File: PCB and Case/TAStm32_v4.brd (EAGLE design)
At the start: 50 x 100 mm, 55 parts, among them CN1 330pF, CN2 330pF, CN3 330pF, CN4 330pF, IC1 74HCT3G07DP-Q100H, IC2 74HCT3G07DP-Q100H, IC3 74AVCH4T245PW,118, IC4 74AVCH4T245PW,118, J1 ZX62D-B-5PA8, J10 RJSSE538002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

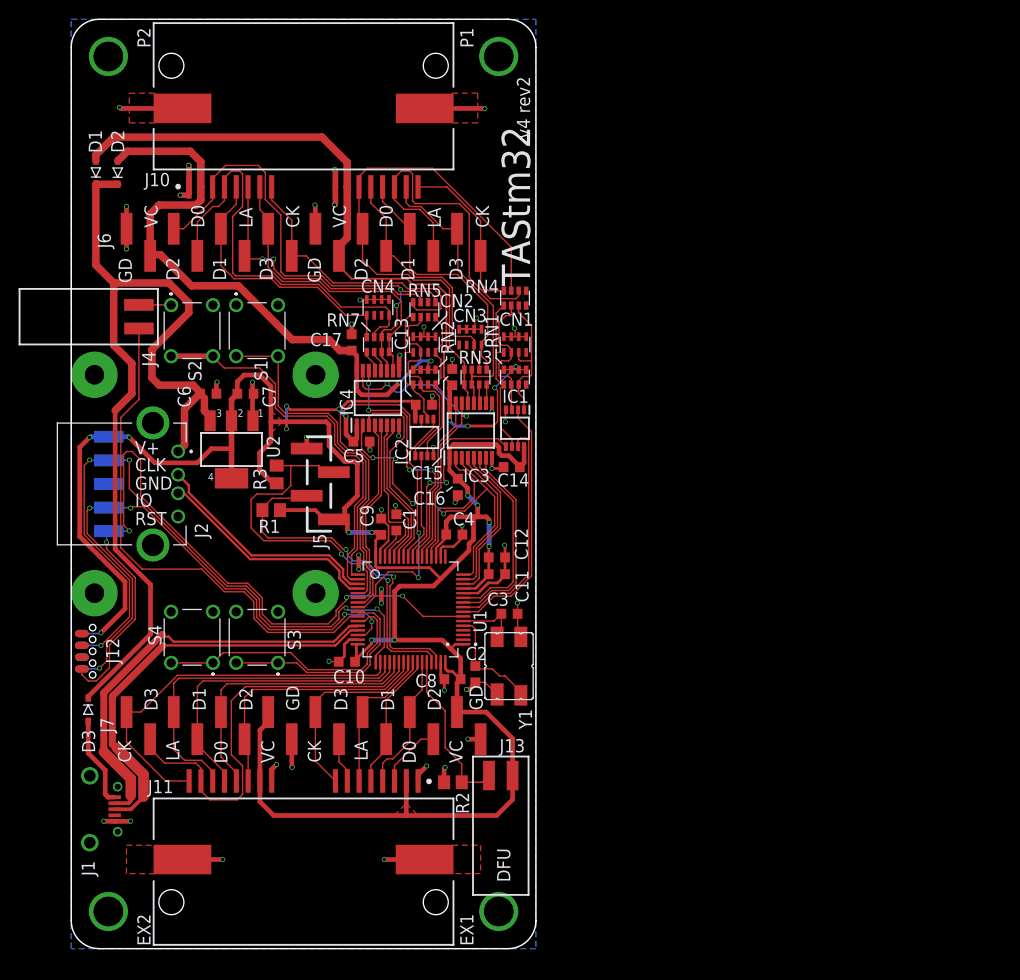
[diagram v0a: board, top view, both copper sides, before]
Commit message: more silkscreen cleanup
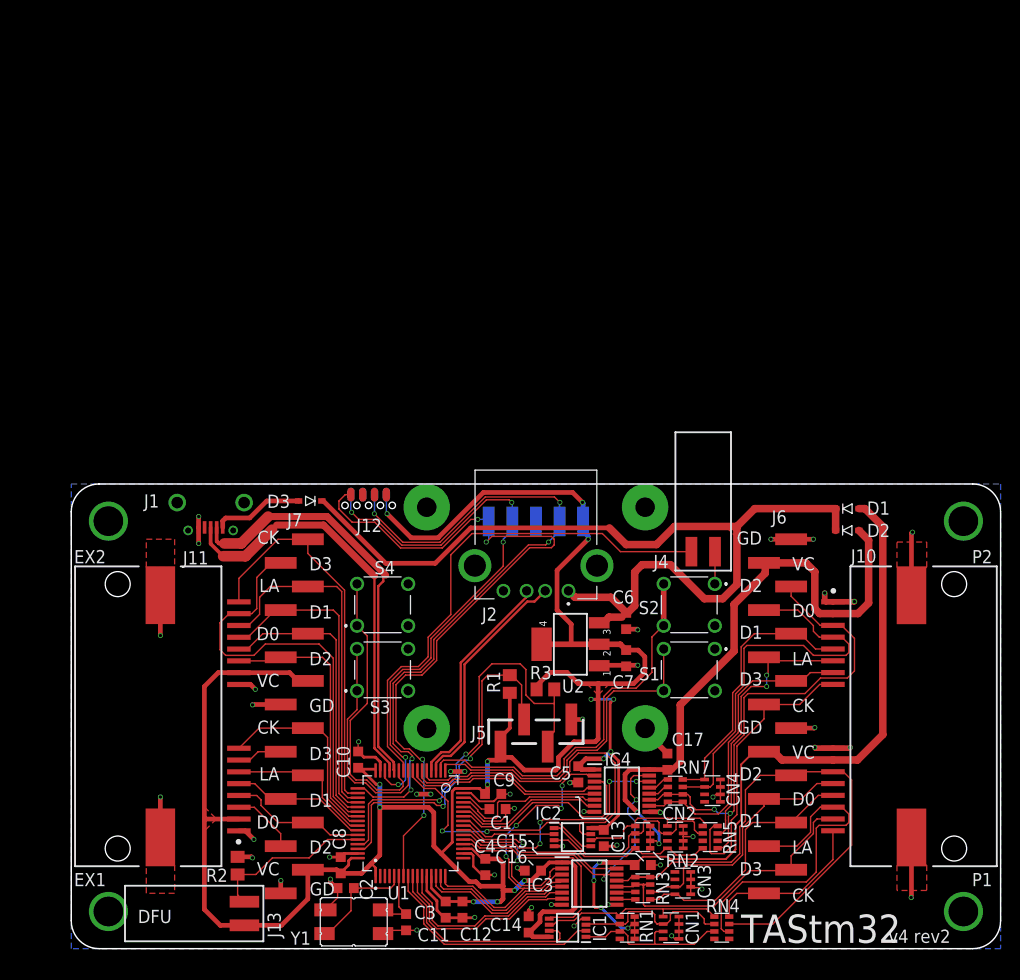
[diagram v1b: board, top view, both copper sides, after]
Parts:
- moved J10 99.0 mm to (95.0, 25.0), turned to 90 degrees
- moved D1 88.6 mm to (83.5, 47.3), turned to 0 degrees
- moved D2 87.4 mm to (83.5, 45.0), turned to 0 degrees
- moved J6 72.1 mm to (76.0, 25.0), turned to 270 degrees
- moved RN4 71.3 mm to (70.0, 2.25), turned to 90 degrees
- moved J4 69.0 mm to (68.0, 48.0), turned to 0 degrees
- moved CN1 65.0 mm to (64.5, 2.25), turned to 180 degrees
- moved RN5 64.5 mm to (68.8, 12.0), turned to 90 degrees
- moved CN4 63.2 mm to (69.0, 17.0), turned to 180 degrees
- moved CN3 63.0 mm to (65.8, 7.05), turned to 180 degrees
- moved S2 61.1 mm to (66.5, 37.0), turned to 0 degrees
- moved RN1 60.5 mm to (59.8, 2.25), turned to 270 degrees
- moved CN2 59.5 mm to (65.0, 12.0), turned to 180 degrees
- moved S1 59.1 mm to (66.5, 30.0), turned to 0 degrees
- moved RN3 57.9 mm to (61.5, 6.50), turned to 270 degrees
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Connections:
- net P2_D0: now also CN4.6; no longer CN4.8
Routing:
- net V+: track 278.3 -> 281.6 mm
- net P1_D2_3V_IN: track 22.0 -> 25.2 mm
- net GND: track 134.8 -> 138.0 mm
- net P2_D0: track 45.9 -> 43.3 mm
- net NRST: track 82.7 -> 80.0 mm
- net N$18: track 15.1 -> 17.7 mm
- net N$17: track 17.5 -> 20.1 mm
- net P1_CLOCK_3V: track 27.4 -> 24.8 mm
- net N$16: track 15.2 -> 17.8 mm
- net P1_VCC: track 83.5 -> 81.1 mm
- net P1_LATCH_3V: track 24.9 -> 22.8 mm
- net P2_LATCH_3V: track 34.3 -> 35.9 mm
- net DIR_D0D1: track 38.0 -> 36.8 mm
- net N$8: track 17.0 -> 18.2 mm
- net N$4: track 21.7 -> 22.9 mm
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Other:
- board size 50 x 100 mm -> 100 x 50 mm

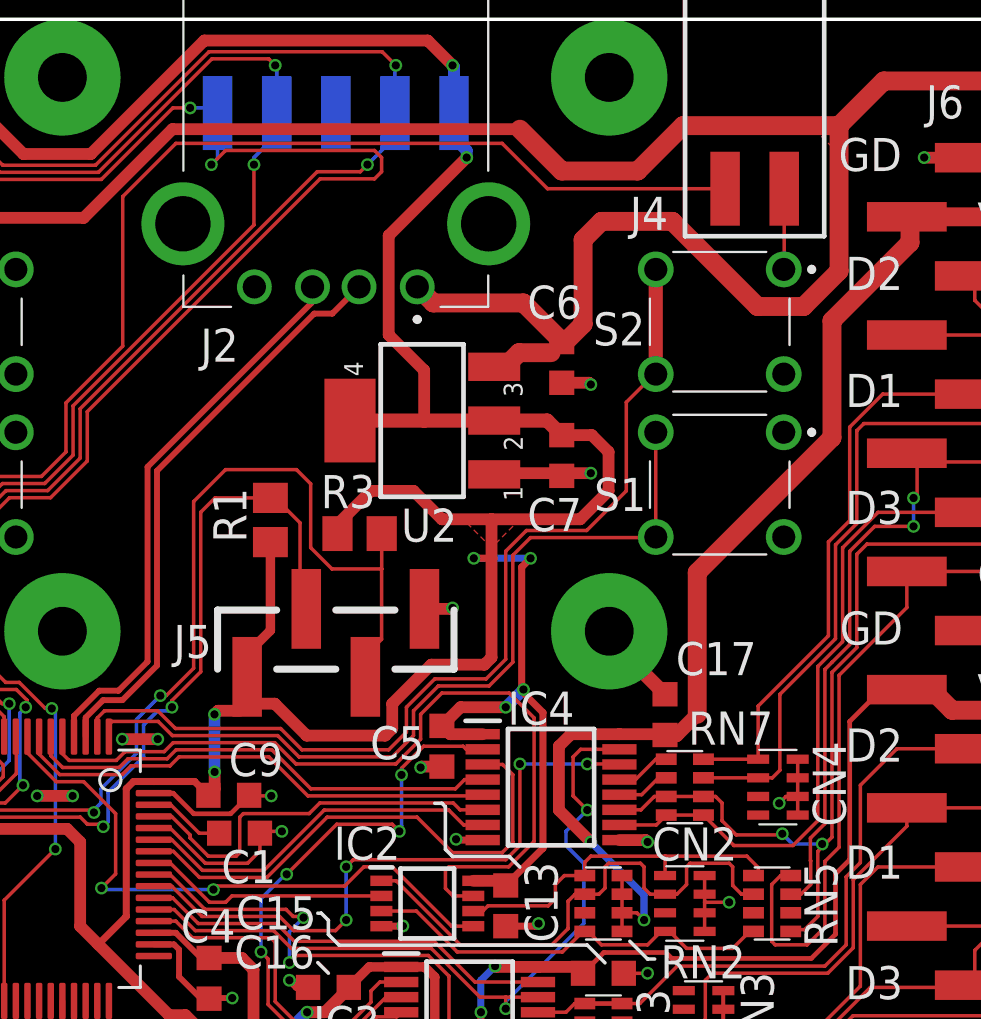
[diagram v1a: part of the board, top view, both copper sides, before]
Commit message: yet more silkscreen cleanup
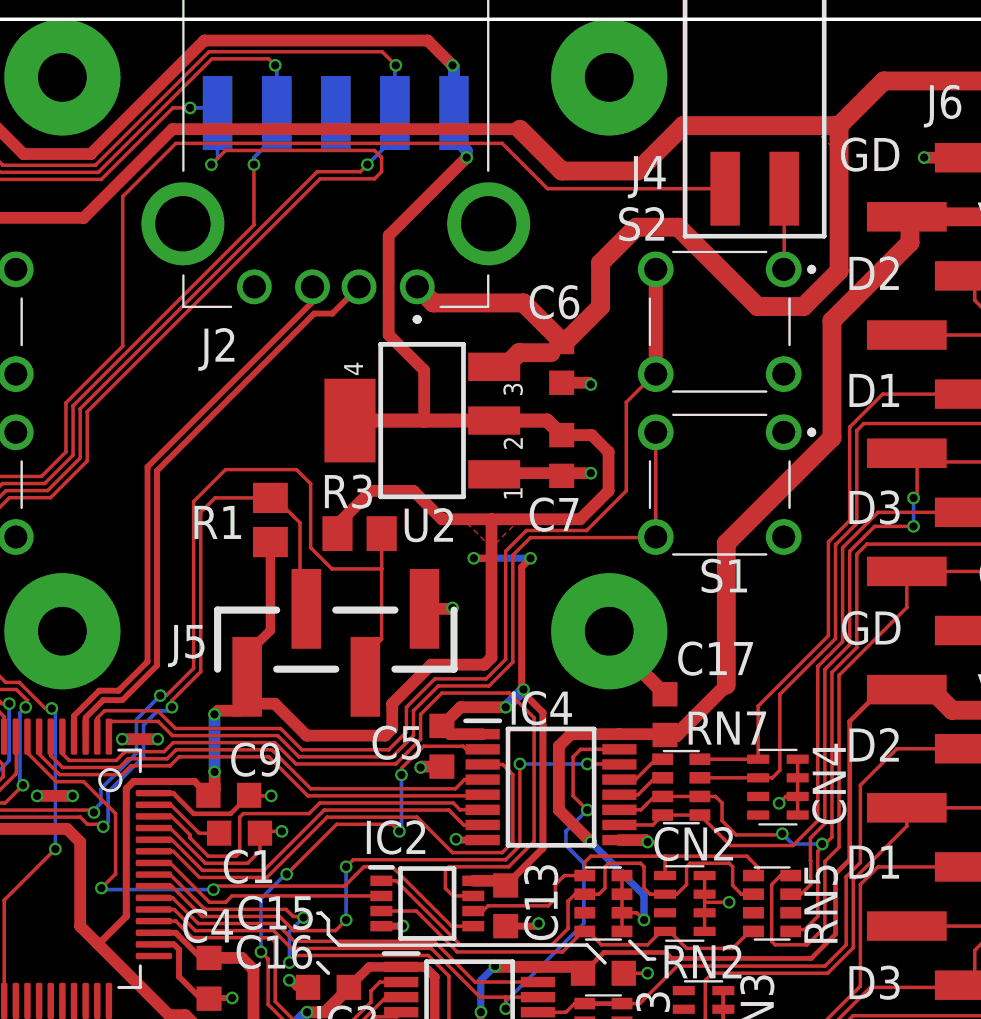
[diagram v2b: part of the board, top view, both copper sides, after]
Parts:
- moved RN7 0.15 mm to (64.8, 17.0)
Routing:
- net +5V: track 99.5 -> 98.3 mm

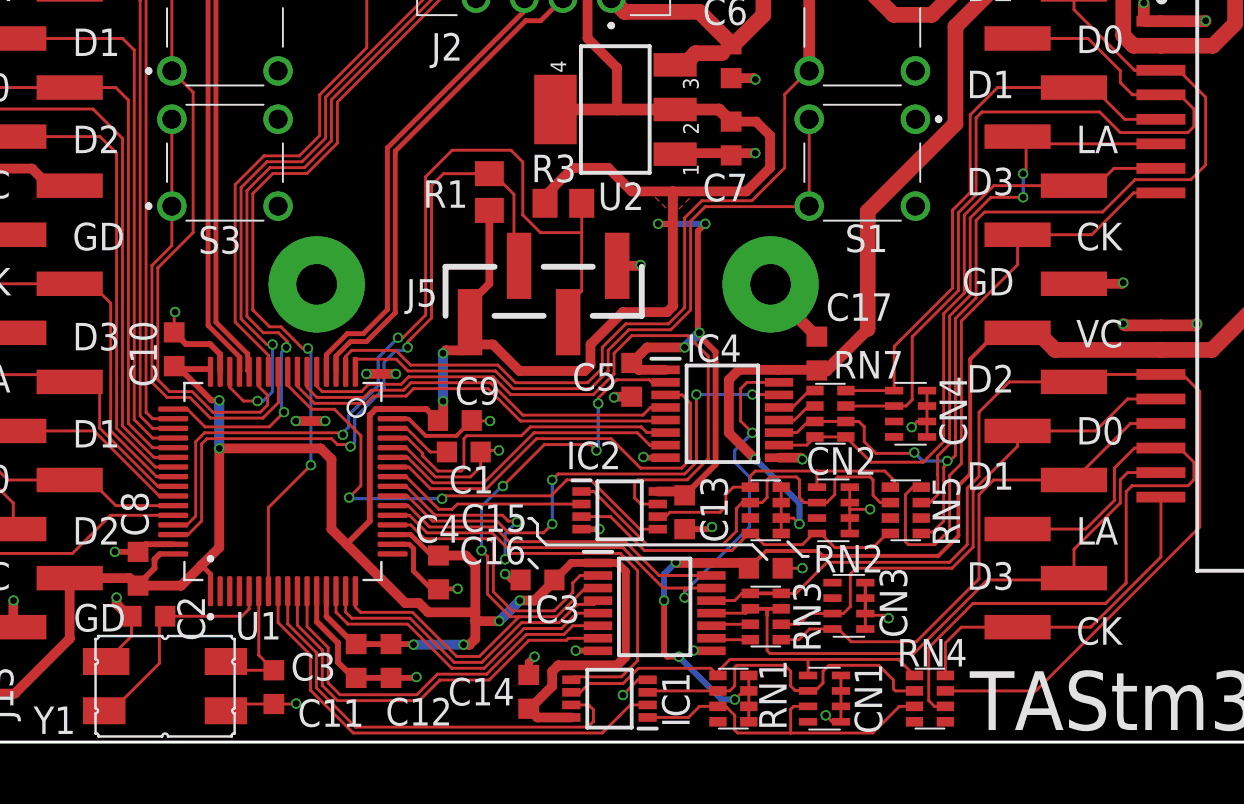
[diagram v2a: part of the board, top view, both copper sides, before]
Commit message: spacing out components
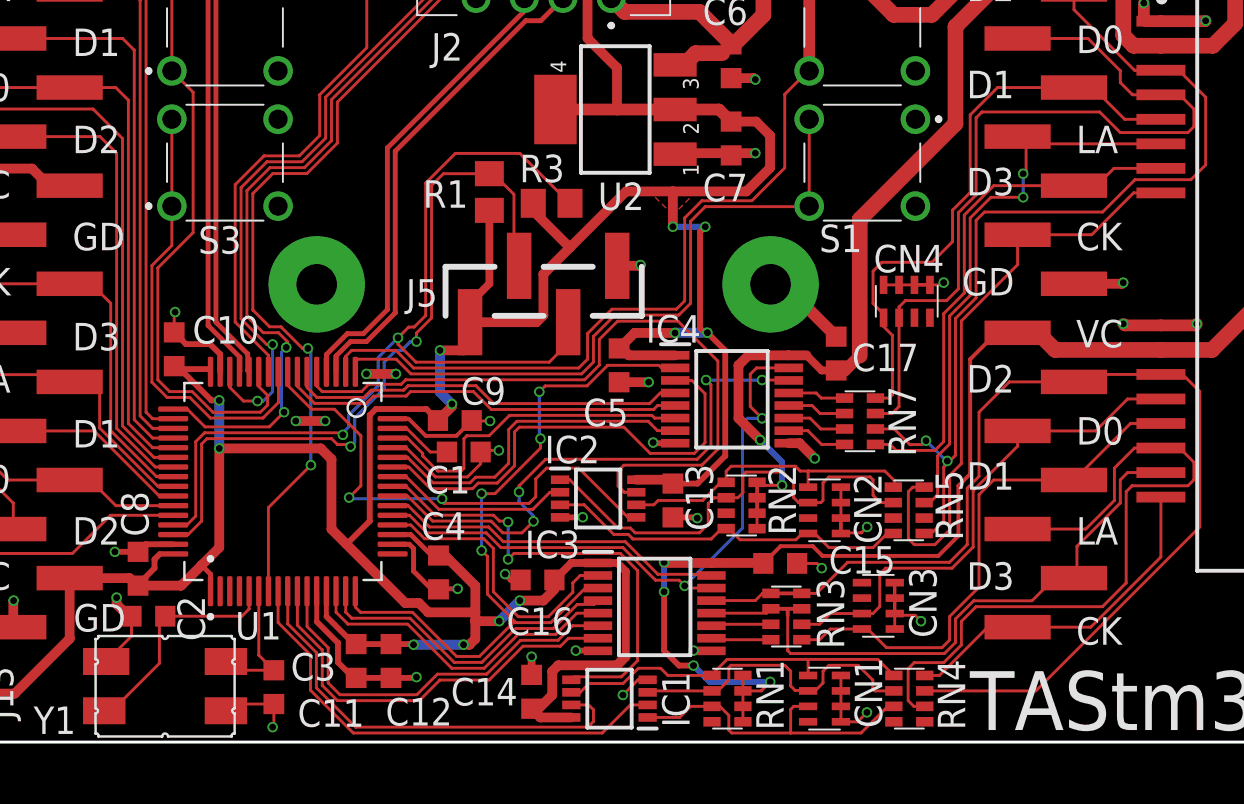
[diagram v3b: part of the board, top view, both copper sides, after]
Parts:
- moved CN4 5.83 mm to (68.8, 22.8), turned to 270 degrees
- moved RN7 1.58 mm to (66.4, 16.6)
- moved CN3 1.52 mm to (67.3, 7.05)
- moved RN2 1.27 mm to (60.2, 12.2)
- moved IC2 1.27 mm to (52.8, 12.6)
- moved RN3 1.07 mm to (62.6, 6.50)
- moved RN4 1.07 mm to (68.9, 2.25)
- moved C17 1.00 mm to (65.1, 20.1)
- moved C5 0.99 mm to (53.9, 19.5)
- moved IC4 0.90 mm to (59.8, 17.8)
- moved C13 0.86 mm to (56.7, 12.5)
- moved C15 0.79 mm to (62.2, 9.25)
- moved R3 0.61 mm to (50.4, 27.9)
- moved CN2 0.46 mm to (64.5, 12.0)
- moved RN1 0.30 mm to (59.5, 2.25)
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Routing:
- net V+: track 281.6 -> 275.9 mm
- net GND: track 138.0 -> 142.4 mm
- net P2_D2: track 54.5 -> 51.7 mm
- net P2_D3: track 33.0 -> 30.4 mm
- net P1_VCC: track 81.1 -> 83.5 mm
- net DIR_P2D2D3: track 22.2 -> 24.1 mm
- net ENABLE_P2D2D3: track 27.2 -> 29.1 mm
- net P2_D3_3V: track 16.0 -> 17.7 mm
- net N$18: track 17.7 -> 16.4 mm
- net DIR_D0D1: track 36.8 -> 38.0 mm
- net N$17: track 20.1 -> 18.9 mm
- net N$4: track 22.9 -> 24.1 mm
- net P1_LATCH: track 36.9 -> 38.0 mm
- net N$16: track 17.8 -> 16.8 mm
- net P1_D2: track 57.9 -> 59.0 mm
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
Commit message: more tidying
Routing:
- net ENABLE_P2D2D3: track 29.1 -> 28.3 mm
- net P1_LATCH: track 38.0 -> 37.3 mm
- net P1_D1: track 27.5 -> 26.9 mm
- net V+: track 275.9 -> 276.5 mm
- net P2_CLOCK: track 31.0 -> 31.6 mm
- net P1_D2: track 59.0 -> 59.5 mm

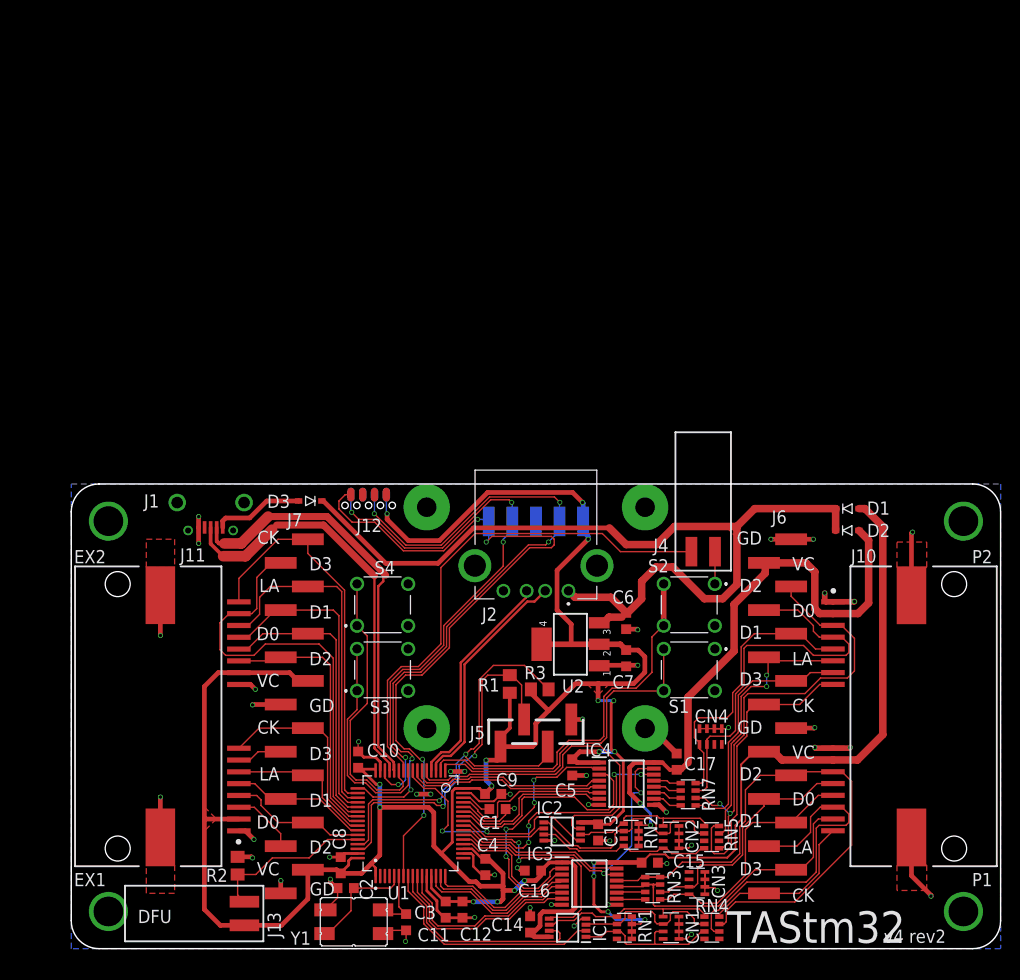
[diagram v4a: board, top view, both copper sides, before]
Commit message: ground fill on top
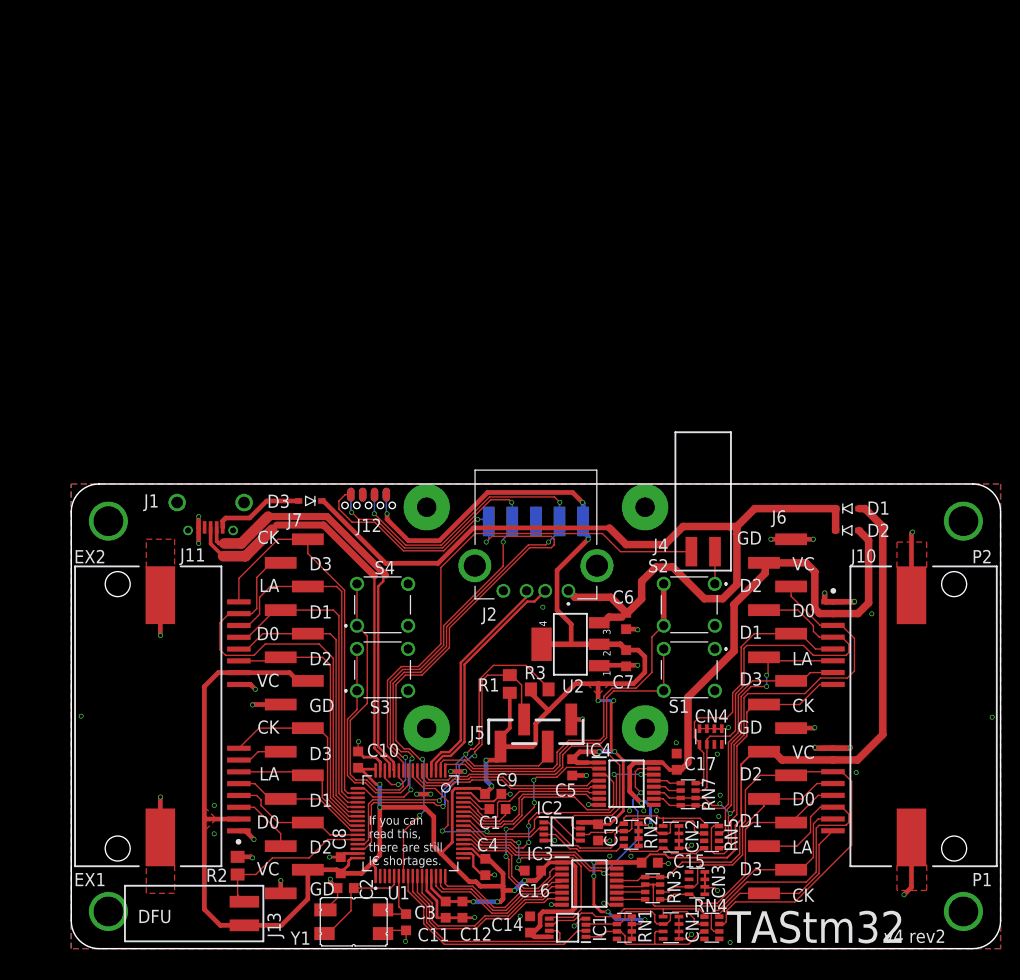
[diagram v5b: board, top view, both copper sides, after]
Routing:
- net GND: track 142.8 -> 136.8 mm, vias 52 -> 69
- net P2_D3: track 30.4 -> 32.0 mm
- net P2_D2: track 51.7 -> 53.3 mm
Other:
- board text added: "If you can read this, there are still IC shortages."
